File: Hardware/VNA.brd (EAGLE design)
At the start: 122 x 96 mm, 502 parts, among them IC1 MIC2253, IC10 MAX2871, IC11 RFSW6042, IC12 RFSW6042, IC13 QPC6324, IC14 RFSA3714, IC15 TRF37A73, IC16 QPC6324, IC17 QPC6324, IC18 QPC6324, IC19 AP2114H, IC2 LM3370SD-4221, IC20 NCP702-3.3, IC21 MAX2871, IC22 LT5560, IC23 THS4521IDGKR, IC24 ADL5801, IC25 NCP702-1.8, IC26 MCP33131D-10-E/MS, IC27 LT5560, IC28 THS4521IDGKR, IC29 ADL5801, IC3 LDL212PU50R, IC30 NCP702-1.8, IC31 MCP33131D-10-E/MS, IC32 THS4521IDGKR, IC33 ADL5801, IC34 NCP702-1.8, IC35 MCP33131D-10-E/MS, IC36 LT5560, IC37 STM32G431CB, IC4 LDL212PU50R, IC5 LDL212PU50R, IC6 LDL212PU50R, IC7 SI5351C, IC8 AP2114H, IC9 NCP702-3.3, J1 DNP, J2 AMPHENOL_132289, J3 AMPHENOL_132289, J4 TYPE-C16P(073), Q1 FA-128 26MHz, T1 B012-617DB-1-63-B331, T2 B012-617DB-1-63-B331, T3 B012-617DB-1-63-B331, U1 W25Q16BVSN, U2 6SLX9TQG144, X1 SMA_CONNECTOR, X2 SMA_CONNECTOR, X3 DNP

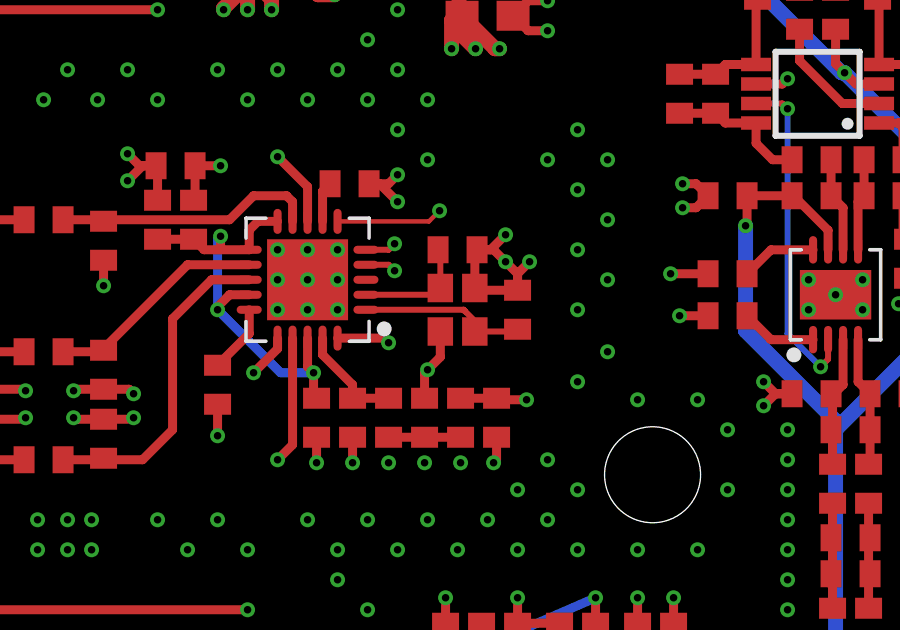
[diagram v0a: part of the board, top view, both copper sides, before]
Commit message: TCXO instead of crystal
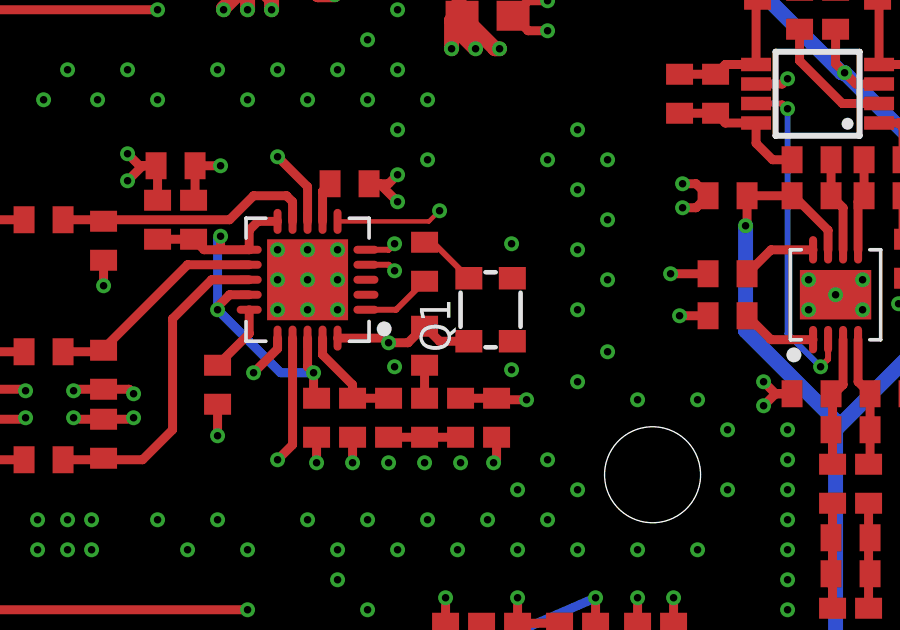
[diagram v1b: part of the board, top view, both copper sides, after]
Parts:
- C31, C34: value 4p -> 100n
- Q1: value FA-128 26MHz -> DSB221SDN/26MHz; device VNA:FA-128 -> crystal-geyer_V1_0:2.5X2.0_KXO-86-TCXO
- moved C34 3.49 mm to (99.9, 42.6), turned to 90 degrees
- moved C31 3.38 mm to (99.9, 39.8), turned to 90 degrees
- moved Q1 1.10 mm to (102.1, 41.0), turned to 90 degrees
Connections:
- net +3V3: now also C31.2, Q1.4
- net GND: now also Q1.1; no longer C34.1, Q1.4
- net N$113: no longer IC7.1
- net N$114: now also C34.1, IC7.1; no longer C31.2, IC7.2, Q1.1
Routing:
- net GND: track 738.6 -> 729.8 mm, vias 1585 -> 1584
- net N$113: track 5.66 -> 1.97 mm
- net +3V3: track 395.7 -> 398.9 mm
- net N$114: track 4.30 -> 2.35 mm
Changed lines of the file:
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@@
 <drawing>
 <settings>
-<setting alwaysvectorfont="yes"/>
+<setting alwaysvectorfont="no"/>
 <setting verticaltext="up"/>
 </settings>
@@
 <layer number="13" name="Route13" color="21" fill="1" visible="no" active="no"/>
 <layer number="14" name="Route14" color="22" fill="1" visible="no" active="no"/>
-<layer number="15" name="Route15" color="14" fill="1" visible="no" active="yes"/>
+<layer number="15" name="Route15" color="14" fill="1" visible="yes" active="yes"/>
 <layer number="16" name="Bottom" color="1" fill="1" visible="yes" active="yes"/>
 <layer number="17" name="Pads" color="2" fill="1" visible="yes" active="yes"/>
@@
 <attribute name="VALUE" x="109.095" y="91.135" size="1.27" layer="27" rot="R270"/>
 </element>
-<element name="C31" library="VNA" library_urn="urn:adsk.eagle:library:22367181" package="C0402" package3d_urn="urn:adsk.eagle:package:22367275/2" value="4p" x="101" y="43" smashed="yes" rot="R180">
-<attribute name="VALUE" x="101.635" y="44.905" size="1.27" layer="27" rot="R180"/>
+<element name="C31" library="VNA" library_urn="urn:adsk.eagle:library:22367181" package="C0402" package3d_urn="urn:adsk.eagle:package:22367275/2" value="100n" x="99.9" y="39.8" smashed="yes" rot="R90">
+<attribute name="VALUE" x="101.805" y="39.165" size="1.27" layer="27" rot="R90"/>
 </element>
-<element name="C34" library="VNA" library_urn="urn:adsk.eagle:library:22367181" package="C0402" package3d_urn="urn:adsk.eagle:package:22367275/2" value="4p" x="103" y="41" smashed="yes" rot="R270">
-<attribute name="VALUE" x="101.095" y="41.635" size="1.27" layer="27" rot="R270"/>
+<element name="C34" library="VNA" library_urn="urn:adsk.eagle:library:22367181" package="C0402" package3d_urn="urn:adsk.eagle:package:22367275/2" value="100n" x="99.9" y="42.6" smashed="yes" rot="R90">
+<attribute name="VALUE" x="101.805" y="41.965" size="1.27" layer="27" rot="R90"/>
 </element>
 <element name="C120" library="VNA" library_urn="urn:adsk.eagle:library:22367181" package="C0402" package3d_urn="urn:adsk.eagle:package:22367275/2" value="10n" x="14.7" y="25.6" smashed="yes" rot="R90">
@@
 <attribute name="VALUE" x="57.1109" y="42.1" size="1.27" layer="27" rot="R90" align="top-center"/>
 </element>
-<element name="Q1" library="VNA" library_urn="urn:adsk.eagle:library:22367181" package="FA-128" package3d_urn="urn:adsk.eagle:package:22367298/2" value="FA-128 26MHz" x="101" y="41" smashed="yes" rot="R270">
-<attribute name="VALUE" x="98.46" y="42.27" size="1.27" layer="27" rot="R270"/>
-</element>
 <element name="R41" library="VNA" library_urn="urn:adsk.eagle:library:22367181" package="R0402" package3d_urn="urn:adsk.eagle:package:22367274/2" value="620" x="25.1" y="6.3" smashed="yes" rot="R270">
 <attribute name="VALUE" x="23.195" y="6.935" size="1.27" layer="27" rot="R270"/>
@@
 <attribute name="VALUE" x="90.435" y="80.905" size="1.27" layer="27" rot="R180"/>
 </element>
+<element name="Q1" library="crystal-geyer_V1_0" library_urn="urn:adsk.eagle:library:203" package="2.5X2.0_KXO-86-TCXO" package3d_urn="urn:adsk.eagle:package:11955/1" value="DSB221SDN/26MHz" x="102.1" y="41" smashed="yes" rot="R90">
+<attribute name="NAME" x="100.762" y="39.589" size="1.016" layer="25" rot="R90"/>
+<attribute name="VALUE" x="104.484" y="39.589" size="1.016" layer="27" rot="R90"/>
+</element>
 </elements>
 <signals>
@@
 <contactref element="C33" pad="1"/>
 <contactref element="R6" pad="1"/>
-<contactref element="Q1" pad="2"/>
-<contactref element="C31" pad="1"/>
-<contactref element="C34" pad="1"/>
-<contactref element="Q1" pad="4"/>
 <contactref element="C29" pad="1"/>
 <contactref element="C35" pad="2"/>
@@
 <via x="101.1" y="35.9" extent="1-16" drill="0.25"/>
 <via x="102.2" y="35.9" extent="1-16" drill="0.25"/>
-<via x="102.6" y="43.5" extent="1-16" drill="0.25"/>
-<via x="102.6" y="42.6" extent="1-16" drill="0.25"/>
-<via x="103.4" y="42.6" extent="1-16" drill="0.25"/>
 <via x="99" y="45.5" extent="1-16" drill="0.25"/>
 <via x="99" y="44.6" extent="1-16" drill="0.25"/>
@@
 <wire x1="96.3" y1="36.75" x2="96.3" y2="35.9" width="0.3" layer="1"/>
 <wire x1="97.5" y1="36.75" x2="97.5" y2="35.9" width="0.3" layer="1"/>
-<wire x1="99.9" y1="38.05" x2="99.9" y2="38.9" width="0.3" layer="1"/>
-<wire x1="99.9" y1="38.9" x2="100" y2="39" width="0.3" layer="1"/>
-<via x="100" y="39" extent="1-16" drill="0.25"/>
-<wire x1="100.425" y1="40.275" x2="100.425" y2="39.425" width="0.3" layer="1"/>
-<wire x1="100.425" y1="39.425" x2="100" y2="39" width="0.3" layer="1"/>
 <wire x1="102.3" y1="36.75" x2="102.3" y2="36" width="0.3" layer="1"/>
 <wire x1="102.3" y1="36" x2="102.2" y2="35.9" width="0.3" layer="1"/>
-<wire x1="103" y1="41.65" x2="101.65" y2="41.65" width="0.3" layer="1"/>
-<wire x1="101.65" y1="41.65" x2="101.575" y2="41.725" width="0.3" layer="1"/>
-<wire x1="101.575" y1="41.725" x2="101.575" y2="42.925" width="0.3" layer="1"/>
-<wire x1="101.575" y1="42.925" x2="101.65" y2="43" width="0.3" layer="1"/>
-<wire x1="101.65" y1="43" x2="102.2" y2="43" width="0.3" layer="1"/>
-<wire x1="102.2" y1="43" x2="102.5" y2="42.7" width="0.3" layer="1"/>
-<wire x1="102.5" y1="42.7" x2="102.6" y2="42.6" width="0.3" layer="1"/>
-<wire x1="101.65" y1="43" x2="102.1" y2="43" width="0.3" layer="1"/>
-<wire x1="102.1" y1="43" x2="102.6" y2="43.5" width="0.3" layer="1"/>
-<wire x1="103" y1="41.65" x2="103" y2="42.2" width="0.3" layer="1"/>
-<wire x1="103" y1="42.2" x2="102.5" y2="42.7" width="0.3" layer="1"/>
-<wire x1="103" y1="41.65" x2="103" y2="42.2" width="0.3" layer="1"/>
-<wire x1="103" y1="42.2" x2="103.4" y2="42.6" width="0.3" layer="1"/>
 <wire x1="94.9" y1="6.95" x2="94.9" y2="7.9" width="0.3" layer="1"/>
 <via x="94.9" y="7.9" extent="1-16" drill="0.25"/>
@@
 <vertex x="-4.1" y="-3.7"/>
 </polygon>
+<contactref element="Q1" pad="2"/>
+<contactref element="Q1" pad="1"/>
+<contactref element="C31" pad="1"/>
+<wire x1="99.9" y1="38.05" x2="99.9" y2="39.15" width="0.3" layer="1"/>
+<via x="98.9" y="39.1" extent="1-16" drill="0.25"/>
+<via x="102.8" y="43.2" extent="1-16" drill="0.25"/>
+<via x="102.8" y="39" extent="1-16" drill="0.25"/>
 </signal>
 <signal name="SOURCE_REF">
@@
 <wire x1="96.5" y1="44.95" x2="96.75" y2="45.2" width="0.3" layer="1"/>
 </signal>
-<signal name="N$113">
-<contactref element="C34" pad="2"/>
-<contactref element="Q1" pad="3"/>
-<contactref element="IC7" pad="1"/>
-<wire x1="101.575" y1="40.625" x2="101.575" y2="40.275" width="0.2" layer="1"/>
-<wire x1="101.2" y1="41" x2="101.25" y2="40.95" width="0.2" layer="1"/>
-<wire x1="101.25" y1="40.95" x2="101.575" y2="40.625" width="0.2" layer="1"/>
-<wire x1="97.9456" y1="41" x2="101.2" y2="41" width="0.2" layer="1"/>
-<wire x1="101.2" y1="41" x2="101.25" y2="40.95" width="0.2" layer="1"/>
-<wire x1="101.575" y1="40.275" x2="102.925" y2="40.275" width="0.2" layer="1"/>
-<wire x1="102.925" y1="40.275" x2="103" y2="40.35" width="0.2" layer="1"/>
-</signal>
-<signal name="N$114">
-<contactref element="Q1" pad="1"/>
-<contactref element="C31" pad="2"/>
-<contactref element="IC7" pad="2"/>
-<wire x1="100.2" y1="41.5" x2="100.425" y2="41.725" width="0.3" layer="1"/>
-<wire x1="100.425" y1="42.925" x2="100.35" y2="43" width="0.3" layer="1"/>
-<wire x1="97.9456" y1="41.5" x2="100.2" y2="41.5" width="0.2" layer="1"/>
-<wire x1="100.2" y1="41.5" x2="100.425" y2="41.725" width="0.2" layer="1"/>
-<wire x1="100.425" y1="41.725" x2="100.425" y2="42.925" width="0.2" layer="1"/>
-<wire x1="100.425" y1="42.925" x2="100.35" y2="43" width="0.2" layer="1"/>
-</signal>
 <signal name="N$109">
 <contactref element="L10" pad="2"/>
@@
 <wire x1="74.6" y1="74.8" x2="75.3" y2="74.1" width="0.8128" layer="1"/>
 <wire x1="75.3" y1="74.1" x2="75.3" y2="73.4" width="0.8128" layer="1"/>
+<contactref element="Q1" pad="4"/>
+<contactref element="C31" pad="2"/>
+<wire x1="101.375" y1="39.95" x2="100.4" y2="39.95" width="0.3" layer="1"/>
+<wire x1="100.4" y1="39.95" x2="99.9" y2="40.45" width="0.3" layer="1"/>
+<wire x1="98.7" y1="39.9" x2="99.35" y2="39.9" width="0.3" layer="1"/>
+<wire x1="99.35" y1="39.9" x2="99.9" y2="40.45" width="0.3" layer="1"/>
 </signal>
 <signal name="SCL">
@@
 <wire x1="97.75" y1="73.5" x2="97.05" y2="72.8" width="0.2" layer="1"/>
 </signal>
+<signal name="N$113">
+<contactref element="Q1" pad="3"/>
+<contactref element="C34" pad="2"/>
+<wire x1="101.375" y1="42.05" x2="100.175" y2="43.25" width="0.2" layer="1"/>
+<wire x1="100.175" y1="43.25" x2="99.9" y2="43.25" width="0.2" layer="1"/>
+</signal>
+<signal name="N$114">
+<contactref element="IC7" pad="1"/>
+<contactref element="C34" pad="1"/>
+<wire x1="97.9456" y1="41" x2="98.95" y2="41" width="0.2" layer="1"/>
+<wire x1="98.95" y1="41" x2="99.9" y2="41.95" width="0.2" layer="1"/>
+</signal>
 </signals>

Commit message: GND cutouts under RF component pads
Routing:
- net GND_CUTOUT: track 0.00 -> 1.60 mm
- added copper zone on layer 2, net GND_CUTOUT

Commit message: R27 value fixed
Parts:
- R27: value 406 -> 402
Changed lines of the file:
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@@
 <attribute name="VALUE" x="59.095" y="11.635" size="1.27" layer="27" rot="R270"/>
 </element>
-<element name="R27" library="VNA" library_urn="urn:adsk.eagle:library:22367181" package="R0402" package3d_urn="urn:adsk.eagle:package:22367274/2" value="406" x="60.3" y="12.7" smashed="yes">
+<element name="R27" library="VNA" library_urn="urn:adsk.eagle:library:22367181" package="R0402" package3d_urn="urn:adsk.eagle:package:22367274/2" value="402" x="60.3" y="12.7" smashed="yes">
 <attribute name="VALUE" x="59.665" y="10.795" size="1.27" layer="27"/>
 </element>

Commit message: Trace for port switch moved to fix short with aluminium shield
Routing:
- net PORTSWITCH2: track 70.9 -> 71.5 mm, vias 3 -> 4
- net PORTSWITCH1: track 70.9 -> 70.6 mm, vias 3 -> 4
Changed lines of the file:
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@@
 <via x="59.4" y="5.4" extent="1-16" drill="0.25"/>
 <contactref element="U2" pad="P6"/>
-<wire x1="59.4" y1="5.4" x2="59.4" y2="11.094975" width="0.2" layer="16"/>
-<wire x1="59.4" y1="11.094975" x2="58.144975" y2="12.35" width="0.2" layer="16"/>
 <wire x1="39" y1="34" x2="37" y2="34" width="0.2" layer="16"/>
 <via x="37" y="34" extent="1-16" drill="0.25"/>
-<wire x1="58.144975" y1="12.35" x2="53.65" y2="12.35" width="0.2" layer="16"/>
-<wire x1="53.65" y1="12.35" x2="50.5" y2="15.5" width="0.2" layer="16"/>
-<wire x1="50.5" y1="15.5" x2="50.5" y2="22.5" width="0.2" layer="16"/>
 <wire x1="50.5" y1="22.5" x2="39" y2="34" width="0.2" layer="16"/>
 <via x="28.7" y="57.2" extent="1-16" drill="0.25"/>
@@
 <wire x1="33.8" y1="41.7" x2="33.8" y2="37.2" width="0.15" layer="15"/>
 <wire x1="33.8" y1="37.2" x2="37" y2="34" width="0.15" layer="15"/>
+<wire x1="59.4" y1="5.4" x2="59.4" y2="5.7" width="0.2" layer="15"/>
+<wire x1="50.5" y1="10.6" x2="50.5" y2="11.3" width="0.2" layer="15"/>
+<via x="50.5" y="11.3" extent="1-16" drill="0.25"/>
+<wire x1="59.4" y1="5.7" x2="56.6" y2="8.5" width="0.2" layer="15"/>
+<wire x1="56.6" y1="8.5" x2="52.6" y2="8.5" width="0.2" layer="15"/>
+<wire x1="52.6" y1="8.5" x2="50.5" y2="10.6" width="0.2" layer="15"/>
+<wire x1="50.5" y1="11.3" x2="50.5" y2="22.5" width="0.2" layer="16"/>
 </signal>
 <signal name="N$185">
@@
 <via x="58.7" y="5.4" extent="1-16" drill="0.25"/>
 <contactref element="U2" pad="P7"/>
-<wire x1="58.7" y1="5.4" x2="58.7" y2="11.3" width="0.2" layer="16"/>
 <wire x1="39.5" y1="33" x2="37" y2="33" width="0.2" layer="16"/>
 <via x="37" y="33" extent="1-16" drill="0.25"/>
-<wire x1="58.7" y1="11.3" x2="58" y2="12" width="0.2" layer="16"/>
-<wire x1="58" y1="12" x2="53.5" y2="12" width="0.2" layer="16"/>
-<wire x1="53.5" y1="12" x2="49.5" y2="16" width="0.2" layer="16"/>
-<wire x1="49.5" y1="16" x2="49.5" y2="23" width="0.2" layer="16"/>
 <wire x1="49.5" y1="23" x2="39.5" y2="33" width="0.2" layer="16"/>
 <via x="29.2" y="54.6" extent="1-16" drill="0.25"/>
@@
 <wire x1="30.675" y1="51.94926875" x2="29.2" y2="53.42426875" width="0.15" layer="15"/>
 <wire x1="34.775" y1="43.59884375" x2="30.675" y2="47.69884375" width="0.15" layer="15"/>
+<wire x1="58.7" y1="5.4" x2="56.9" y2="7.2" width="0.2" layer="15"/>
+<wire x1="56.9" y1="7.2" x2="51.8" y2="7.2" width="0.2" layer="15"/>
+<wire x1="51.8" y1="7.2" x2="49.2" y2="9.8" width="0.2" layer="15"/>
+<wire x1="49.2" y1="9.8" x2="49.2" y2="11.3" width="0.2" layer="15"/>
+<via x="49.2" y="11.3" extent="1-16" drill="0.25"/>
+<wire x1="49.2" y1="11.3" x2="49.5" y2="11.6" width="0.2" layer="16"/>
+<wire x1="49.5" y1="11.6" x2="49.5" y2="23" width="0.2" layer="16"/>
 </signal>
 <signal name="PORT1SWITCH">

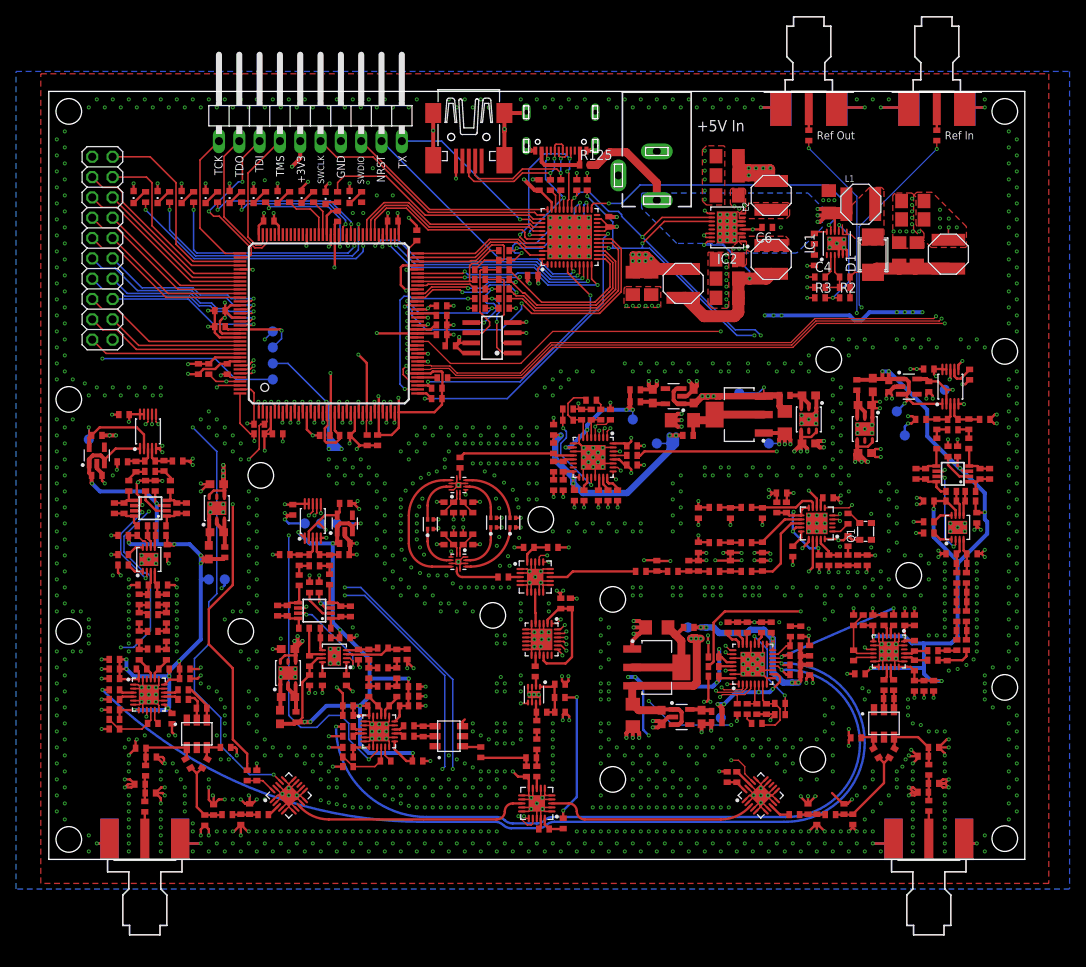
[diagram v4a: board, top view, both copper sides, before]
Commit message: Footprint adjustments for THS4521/0402 inductors, fixed mixup of CCLK/DIN
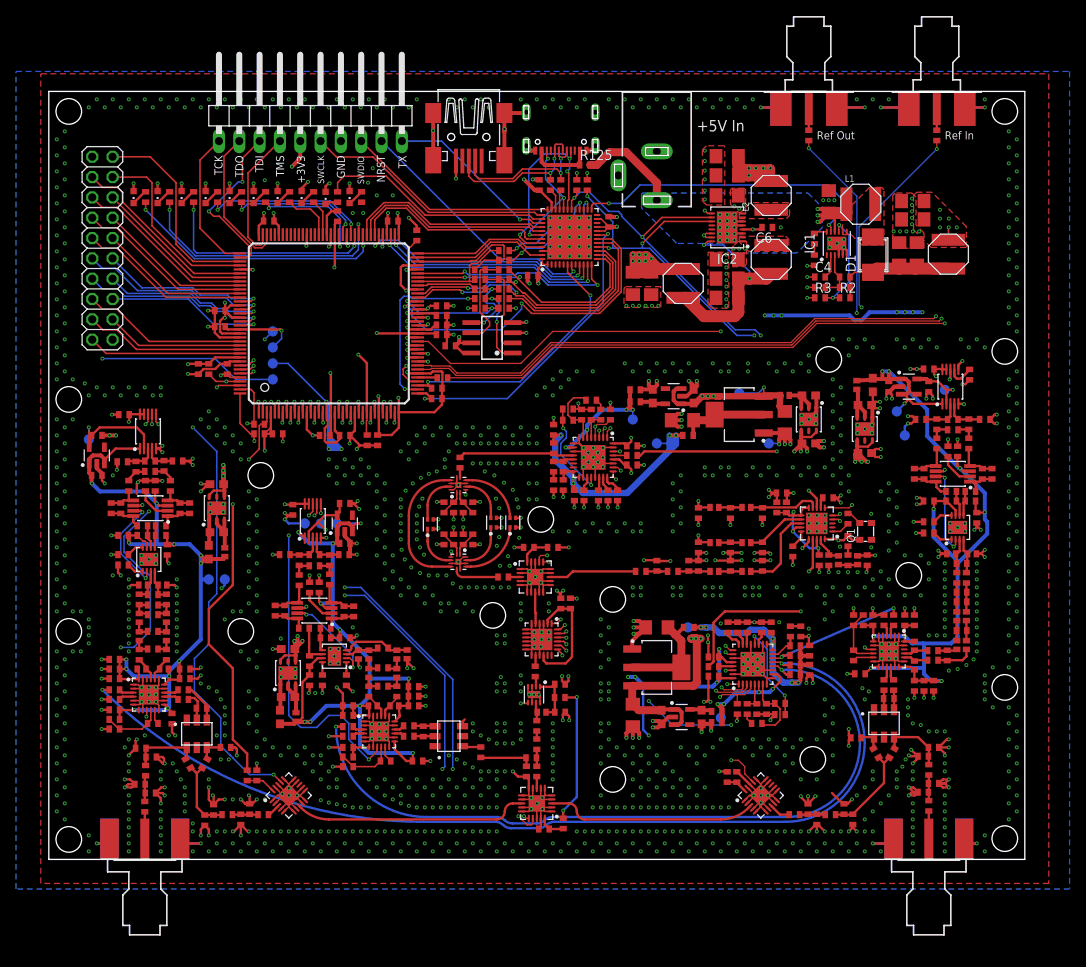
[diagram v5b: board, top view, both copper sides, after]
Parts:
- IC23, IC28, IC32: device VNA:MSOP8 -> VNA:SOP65P490X110-8N
- L10, L19, L20, L21, L22, L23, L25, L26, L27, L28, L29: device VNA:R0402:1 -> VNA:R0402
- L11, L12, L13, L14, L15, L16, L17, L18, L24, L30, L31, L32, L33, L34, L35, L36, L37, L38, L39, L40, L41, L42, L43, L44, L45, L46, L47, L48, L49, L50, L51, L52, L53, L6, L7, L8, L9: device VNA:R0402:1 -> VNA:L0402
- moved C113 0.40 mm to (17.6, 43.9)
- moved R55 0.40 mm to (9.00, 43.9)
- moved C112 0.40 mm to (7.80, 43.9)
- moved C174 0.40 mm to (38.1, 31.0)
- moved R56 0.40 mm to (16.4, 43.9)
- moved R95 0.40 mm to (36.9, 31.0)
- moved C150 0.30 mm to (117.9, 48.2)
- moved C173 0.30 mm to (28.3, 31.1)
- moved R94 0.30 mm to (29.5, 31.1)
- moved R83 0.30 mm to (116.7, 48.2)
- moved R82 0.20 mm to (108.2, 48.2)
- moved C149 0.20 mm to (109.4, 48.2)
- turned IC23 to 180 degrees
- turned IC28 to 180 degrees
- turned IC32 to 180 degrees
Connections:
- net MCU_FPGA_CCLK: now also IC37.26; no longer IC37.28
- net MCU_FPGA_DIN: now also IC37.28; no longer IC37.26
- net N$86: now also IC36.4; no longer IC36.3
- net N$87: now also IC36.3; no longer IC36.4
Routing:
- net MCU_FPGA_DIN: track 15.6 -> 13.9 mm
- net N$86: track 8.13 -> 9.03 mm
- net MCU_FPGA_CCLK: track 16.9 -> 16.1 mm
- net N$92: track 3.85 -> 4.48 mm
- net GND: track 729.8 -> 729.2 mm
- net N$87: track 4.02 -> 4.53 mm
